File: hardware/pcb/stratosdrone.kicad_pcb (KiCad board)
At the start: 4 copper layers, 38 x 74 mm, 115 parts, among them J1 BATT_PH2, J10 DBG, J11 C6DBG, J2 USB-C-16P, J3 FLOW_HDR, J4 CAM_FFC15, J5 MOTOR1, J6 MOTOR2, J7 MOTOR3, J8 MOTOR4, J9 EXP, Q1 AO3400A, Q2 AO3400A, Q3 AO3400A, Q4 AO3400A, SW1 RESET, SW2 BOOT, U1 ESP32-P4NRW32, U10 TLV62569DBVR, U2 W25Q128JVSIQ, U3 ESP32-C6-MINI-1, U4 TP4056-42-ESOP8, U5 SY8089AAAC, U6 ICM-42688-P, U7 SPL06-001, U8 VL53L1X, U9 PMW3901MB, Y1 40MHz

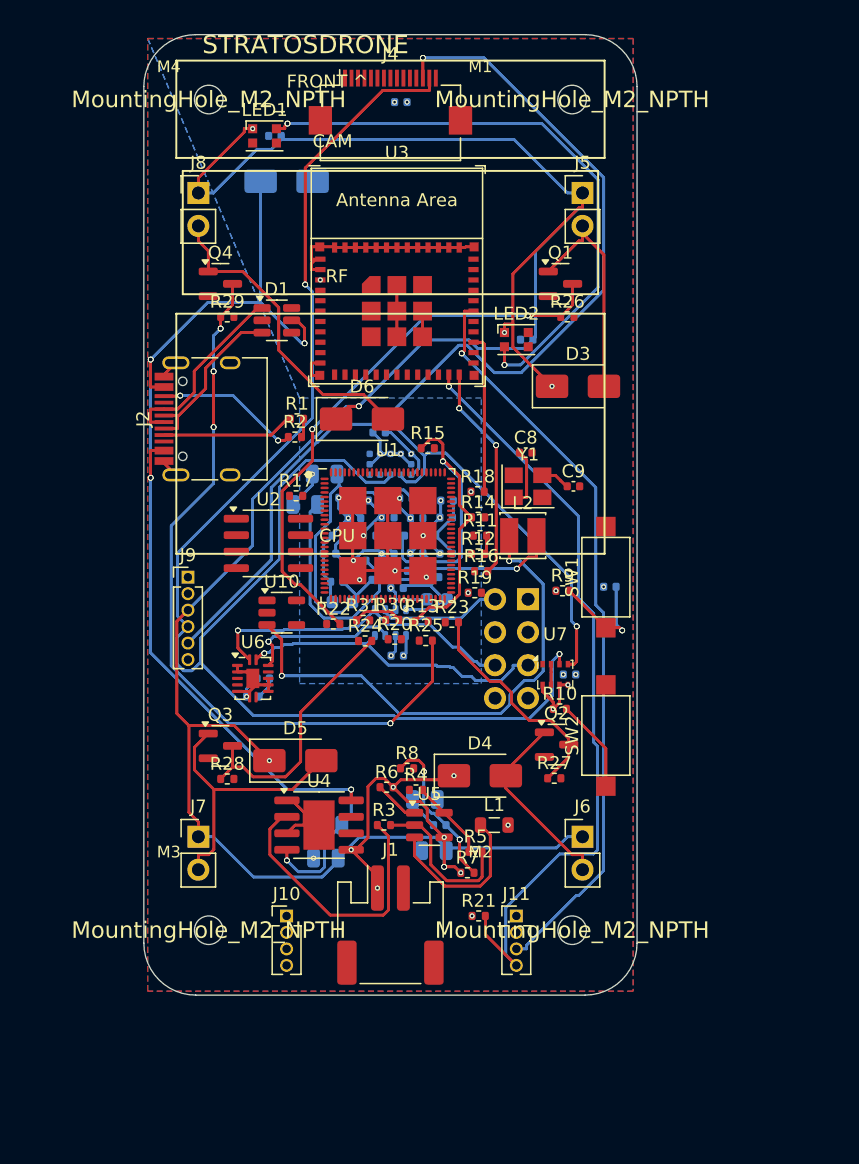
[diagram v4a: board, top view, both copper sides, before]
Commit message: 3-D Eiffel-truss arms; move PCB mount holes into the corners
Two changes spanning the frame and the PCB.

Frame (tello_style/body_bottom.scad):
- Arms are now a real 3-D truss: triangular windows are cut on the top/bottom
  faces (through Z) AND the side faces (through Y), offset by half a bay so the
  cuts interleave. The Eiffel lattice now reads from above and from the front/
  side, not just top-down. Arm raised to 6.5 mm to give the side truss room.
- PCB bosses moved to the new corner pitch (30 x 66) with the filleted/lead-in
  tidy-up kept.

PCB — mount holes relocated to the corners (user request, "trous dans les coins"):
- design.py BOARD mount_pitch 28x64 -> 30x66, i.e. holes at (4,4)/(34,4)/(4,70)/
  (34,70) — centred in each corner_r=4 fillet, a clean classic 4-corner pattern.
- Moved the four MountingHole footprints in the already-routed board in place
  (the corners were verified clear of copper), so the full routing is preserved
  (1384 segments / 121 vias unchanged). Zones refilled, gerbers + drill
  re-exported — NPTH drill now reads X4Y-4 / X34Y-4 / X4Y-70 / X34Y-70.

Frame STL + previews regenerated; README + gen_pcb comment updated. Frame ≈ 25.7 g.

Co-Authored-By: Claude Opus 4.8 <noreply@anthropic.com>
Claude-Session: https://claude.ai/code/session_011szEEHZ8KTTsZmGFgY6Cjw
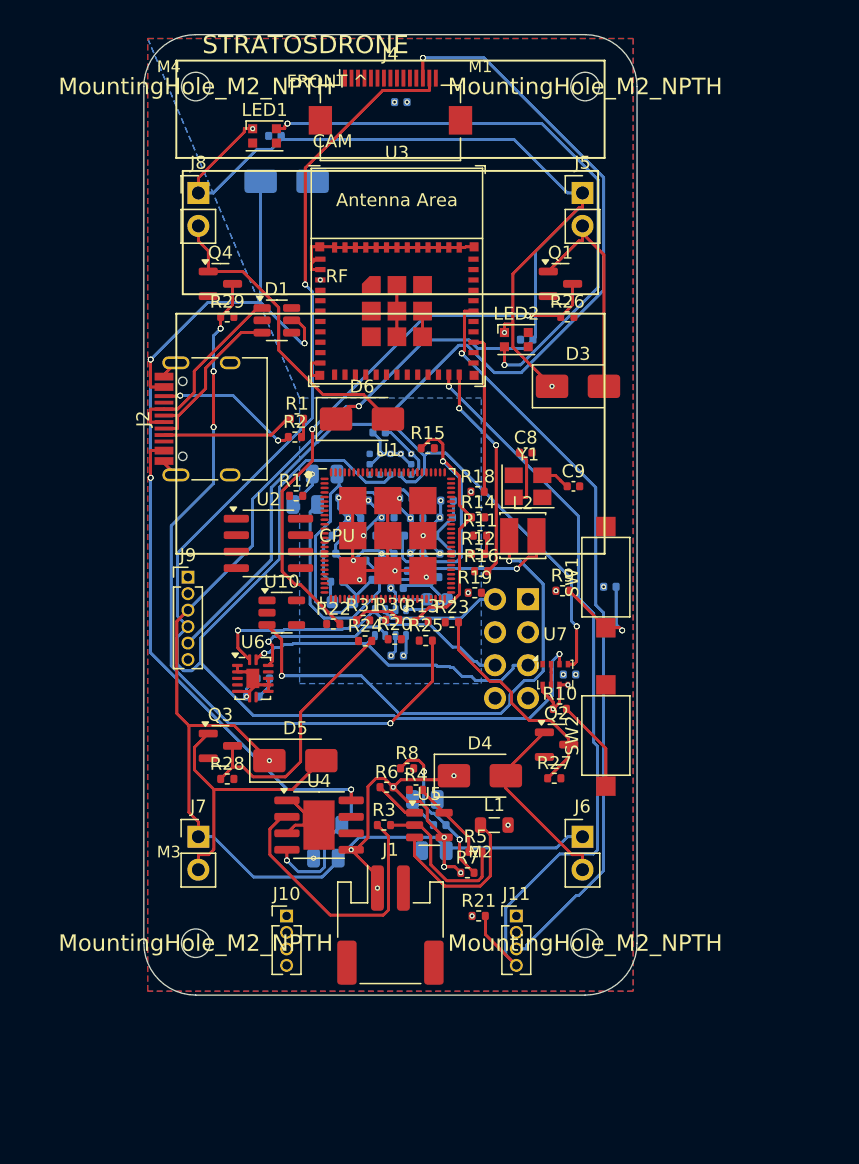
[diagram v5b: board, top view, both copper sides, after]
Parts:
- moved MH1 1.41 mm to (4.00, 4.00)
- moved MH2 1.41 mm to (4.00, 70.0)
- moved MH3 1.41 mm to (34.0, 4.00)
- moved MH4 1.41 mm to (34.0, 70.0)
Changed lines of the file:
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@@
   )
   (footprint "MountingHole:MountingHole_2.2mm_M2" (layer "F.Cu")
-    (at 33 5)
+    (at 34 4)
     (attr exclude_from_pos_files exclude_from_bom)
     (fp_text reference "MH3" (at 0 0) (layer "F.SilkS") hide
@@
   )
   (footprint "MountingHole:MountingHole_2.2mm_M2" (layer "F.Cu")
-    (at 5 69)
+    (at 4 70)
     (attr exclude_from_pos_files exclude_from_bom)
     (fp_text reference "MH2" (at 0 0) (layer "F.SilkS") hide
@@
   )
   (footprint "MountingHole:MountingHole_2.2mm_M2" (layer "F.Cu")
-    (at 33 69)
+    (at 34 70)
     (attr exclude_from_pos_files exclude_from_bom)
     (fp_text reference "MH4" (at 0 0) (layer "F.SilkS") hide
@@
   )
   (footprint "MountingHole:MountingHole_2.2mm_M2" (layer "F.Cu")
-    (at 5 5)
+    (at 4 4)
     (attr exclude_from_pos_files exclude_from_bom)
     (fp_text reference "MH1" (at 0 0) (layer "F.SilkS") hide

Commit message: Clean interior, rounded belly; round PCB corners for hole fab margin
Frame (tello_style):
- Arm roots no longer bulge into the interior: each arm is trimmed to the inner
  cavity (difference against inner_cavity) so from inside/top the pod cavity is
  clean and the board bay is unobstructed.
- Rounded belly: the lower shell's bottom edge is filleted (pod_outer hulls a
  quarter-round profile) so the body reads less flat/boxy from the front. Top
  stays flat to meet the canopy.
- Bosses follow the new 26x62 mount pitch.

PCB — give the corner mount holes a generous fab margin (user request):
- Board corners rounded r4 -> r6 (all four corners verified clear of copper),
  holes moved to (6,6)/(32,6)/(6,68)/(32,68) = mount_pitch 26x62. Drill-to-edge
  margin is now 4.9 mm (was 2.9). Edited the 4 edge arcs + 4 edge lines + 4 hole
  footprints in place; outline re-validated as a closed loop, routing preserved
  (1384 segments / 121 vias), zones refilled, gerbers + drill re-exported.
- design.py BOARD + gen_pcb comment + frame bosses updated to match.

Frame ~22.6 g.

Co-Authored-By: Claude Opus 4.8 <noreply@anthropic.com>
Claude-Session: https://claude.ai/code/session_011szEEHZ8KTTsZmGFgY6Cjw
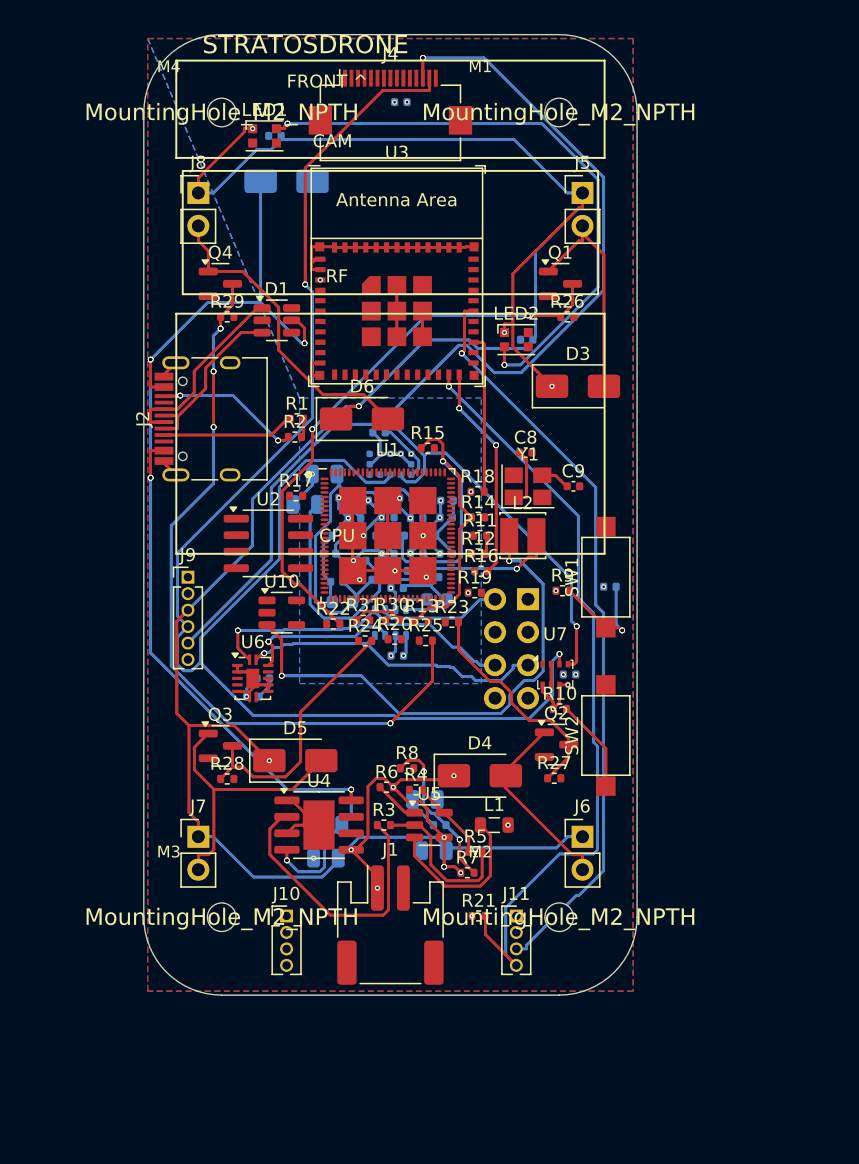
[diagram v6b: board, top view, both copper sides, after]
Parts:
- moved MH1 2.83 mm to (6.00, 6.00)
- moved MH2 2.83 mm to (6.00, 68.0)
- moved MH3 2.83 mm to (32.0, 6.00)
- moved MH4 2.83 mm to (32.0, 68.0)
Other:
- outline, holes or cut-outs redrawn
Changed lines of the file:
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@@
   )
   (footprint "MountingHole:MountingHole_2.2mm_M2" (layer "F.Cu")
-    (at 34 4)
+    (at 32 6)
     (attr exclude_from_pos_files exclude_from_bom)
     (fp_text reference "MH3" (at 0 0) (layer "F.SilkS") hide
@@
   )
   (footprint "MountingHole:MountingHole_2.2mm_M2" (layer "F.Cu")
-    (at 4 70)
+    (at 6 68)
     (attr exclude_from_pos_files exclude_from_bom)
     (fp_text reference "MH2" (at 0 0) (layer "F.SilkS") hide
@@
   )
   (footprint "MountingHole:MountingHole_2.2mm_M2" (layer "F.Cu")
-    (at 34 70)
+    (at 32 68)
     (attr exclude_from_pos_files exclude_from_bom)
     (fp_text reference "MH4" (at 0 0) (layer "F.SilkS") hide
@@
   )
   (footprint "MountingHole:MountingHole_2.2mm_M2" (layer "F.Cu")
-    (at 4 4)
+    (at 6 6)
     (attr exclude_from_pos_files exclude_from_bom)
     (fp_text reference "MH1" (at 0 0) (layer "F.SilkS") hide
@@
   (gr_line (start 35.5 9.5) (end 2.5 9.5)
     (stroke (width 0.15) (type solid)) (layer "F.SilkS"))
-  (gr_arc (start 38 70) (mid 36.828427 72.828427) (end 34 74)
+  (gr_arc (start 38 68) (mid 36.242641 72.242641) (end 32 74)
     (stroke (width 0.1) (type default)) (layer "Edge.Cuts"))
-  (gr_arc (start 34 0) (mid 36.828427 1.171573) (end 38 4)
+  (gr_arc (start 32 0) (mid 36.242641 1.757359) (end 38 6)
     (stroke (width 0.1) (type default)) (layer "Edge.Cuts"))
-  (gr_line (start 38 4) (end 38 70)
+  (gr_line (start 38 6) (end 38 68)
     (stroke (width 0.1) (type default)) (layer "Edge.Cuts"))
-  (gr_line (start 34 74) (end 4 74)
+  (gr_line (start 32 74) (end 6 74)
     (stroke (width 0.1) (type default)) (layer "Edge.Cuts"))
-  (gr_arc (start 4 74) (mid 1.171573 72.828427) (end 0 70)
+  (gr_arc (start 6 74) (mid 1.757359 72.242641) (end 0 68)
     (stroke (width 0.1) (type default)) (layer "Edge.Cuts"))
-  (gr_line (start 4 0) (end 34 0)
+  (gr_line (start 6 0) (end 32 0)
     (stroke (width 0.1) (type default)) (layer "Edge.Cuts"))
-  (gr_arc (start 0 4) (mid 1.171573 1.171573) (end 4 0)
+  (gr_arc (start 0 6) (mid 1.757359 1.757359) (end 6 0)
     (stroke (width 0.1) (type default)) (layer "Edge.Cuts"))
-  (gr_line (start 0 70) (end 0 4)
+  (gr_line (start 0 68) (end 0 6)
     (stroke (width 0.1) (type default)) (layer "Edge.Cuts"))
   (gr_text "FLOW + ToF" (at 9 39) (layer "B.SilkS")
